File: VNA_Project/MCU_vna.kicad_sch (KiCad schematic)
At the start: 53 parts, among them J2 SWD TC2030, J401 Conn_01x04_Pin, J402 Conn_01x04_Pin, J403 Conn_01x04_Pin, J404 Conn_01x04_Pin, J5 Conn_01x04_Pin, SW401 SW_Push, SW402 SW_SPDT, U401 STM32H730VBTx, Y401 NX2016SA25MHz

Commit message: DAC
DAC
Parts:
- added R403: 2k, symbol Device:R
- added R409: 1k, symbol Device:R
- added TP401: TestPoint, symbol Connector:TestPoint
- added U402: TP17-SR, SOIC-8_TPK, symbol 2025-11-02_23-43-44:TP17-SR
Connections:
- net GND: now also R409.1, U402.4 (VS-)
- net DAC1_OUT: now reaches U401.28 (PA4)
- net DAC1_OUT: now also U402.3 (IN+)
- net USB_VBUS: no longer names the net of U401.68 (PA9)
- new net: R403.1, R409.2, U402.2 (IN-)
- new net +10V: U402.7 (VS+)
- new net VCO_TUNE: R403.2, TP401.1, U402.6 (OUT)
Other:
- note added: "Non inverting, G = 1+ R2/R1 = 3, 0-3.3V in 0-9.9V Out"
- note added: "VCO Sweep Generator"

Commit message: finishing up front end
refining Non RF front end
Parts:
- removed C18: 100nF, Capacitor_SMD:C_0402_1005Metric, symbol Device:C
- removed C415, C416: 100n, symbol Device:C
- removed D401, D402, D403, D404, D405, D406: ESD131-B1-W0201, Diode_SMD:Infineon_SG-WLL-2-3_0.58x0.28_P0.36mm, symbol Diode:ESD131-B1-W0201
- removed J2: SWD TC2030, Connector:Tag-Connect_TC2030-IDC-FP_2x03_P1.27mm_Vertical, symbol Connector:Conn_ARM_SWD_TagConnect_TC2030
- removed J401, J402: Conn_01x04_Pin, symbol Connector:Conn_01x04_Pin
- removed R404: 10k, symbol Device:R
- removed R5: 220R, Resistor_SMD:R_0402_1005Metric, symbol Device:R
- removed SW401: SW_Push, symbol Switch:SW_Push
- removed SW402: SW_SPDT, symbol Switch:SW_SPDT
- added C212: 100n, Capacitor_SMD:C_0402_1005Metric, symbol Device:C
- added C45: 100n, symbol Device:C
- added D10, D11, D12, D6, D7, D8: ESD131-B1-W0201, Diode_SMD:Infineon_SG-WLL-2-3_0.58x0.28_P0.36mm, symbol Diode:ESD131-B1-W0201
- added D13, D14, D15, D9: RED, symbol Device:LED
- added J3: 2x5 1.27mm, Connector_PinHeader_1.27mm:PinHeader_2x05_P1.27mm_Vertical_SMD, symbol Connector_Generic:Conn_02x05_Odd_Even
- added LED1: CLMVC-FKA-CL1D1L71BB7C3C3, CLMVC-FKA-CL1D1L71BB7C3C3_CRE, symbol Non_KiCad_Symbols:CLMVC-FKA-CL1D1L71BB7C3C3
- added R210, R211, R212, R213: 49R9, Resistor_SMD:R_0402_1005Metric, symbol Device:R
- added R40: 10k, Resistor_SMD:R_1206_3216Metric_Pad1.30x1.75mm_HandSolder, symbol Device:R
- added R41, R42, R43, R44, R45, R46: 1000, symbol Device:R
- added SW3: SW_SPDT, Button_Switch_THT:SW_Slide_SPDT_Straight_CK_OS102011MS2Q, symbol Switch:SW_SPDT
- R6: value 220R -> 1000; footprint Resistor_SMD:R_0402_1005Metric -> (none)
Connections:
- net UART_RX is gone; now on net GND: R6.2
- net +3.3V: now also C45.1, D10.2 (A2), D11.2 (A2), D12.2 (A2), D6.2 (A2), J3.1 (Pin_1), LED1.1, SW3.3 (C)
- net BOOT0: now also R40.1
- net GND: now also C212.2, C45.2, D10.1 (A1), D11.1 (A1), D12.1 (A1), D6.1 (A1), D7.1 (A1), D8.1 (A1), J3.3 (Pin_3), J3.5 (Pin_5), J3.9 (Pin_9), R41.2, R42.2, R43.2, SW3.1 (A)
- net JTDO: now also R212.1
- net NRST: now also C212.1, R213.1
- net SWCLK: now also R211.1; no longer D3.2 (A2)
- net SWDIO: now also R210.1; no longer D2.2 (A2)
- net debug_led2: now reaches U401.34 (PB0)
- net debug_led2: now also D13.2 (A)
- net debug_led3: now reaches U401.35 (PB1)
- net debug_led3: now also D14.2 (A)
- net debug_led4: now reaches U401.36 (PB2)
- net debug_led4: now also D15.2 (A)
- net debug_led6: now reaches U401.91 (PB5)
- net debug_led6: now also R45.1
- net debug_led7: now reaches U401.95 (PB8)
- net debug_led7: now also R46.1
- net at R6.1: now also D9.1 (K)
- net JTDI renamed debug_led1
- net debug_led1: now also D9.2 (A)
- net JTRST renamed debug_led5
- net debug_led5: now also R44.1
- new net: D14.1 (K), R42.1
- new net: D13.1 (K), R41.1
- new net: LED1.2, R46.2
- new net: D15.1 (K), R43.1
- new net: LED1.4, R44.2
- new net: LED1.3, R45.2
- new net: R40.2, SW3.2 (B)
- new net CONN_NRST: D8.2 (A2), J3.10 (Pin_10), R213.2
- new net CONN_SWCLK: D3.2 (A2), J3.4 (Pin_4), R211.2
- new net CONN_SWDIO: D2.2 (A2), J3.2 (Pin_2), R210.2
- new net CONN_SWO: D7.2 (A2), J3.6 (Pin_6), R212.2
- no-connect marks 1 -> 33
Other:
- note added: "- credit phils lab"
- note added: "1k"
- note added: "25MHZ"
- note added: "DEBUG 1 - Clock DEBUG 2 - ADC DEBUG 3 - DAC DEBUG 4 - ETH DEBUG 5,6,7 - Temperature Stability Gradient"
- note added: "RGB Gradient"
- note removed: "NRST"
- note removed: "SWD 2"
- note removed: "UART"
- moved on the sheet: D407, D408, D409, D410, D411, D412, J403, J404, J5, R403, R405, R406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

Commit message: AA filtering
redoing AA filtering
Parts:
- removed D10, D11, D12, D407, D408, D409, D410, D411, D412: ESD131-B1-W0201, Diode_SMD:Infineon_SG-WLL-2-3_0.58x0.28_P0.36mm, symbol Diode:ESD131-B1-W0201
- removed J403, J404, J5: Conn_01x04_Pin, Connector_PinSocket_2.00mm:PinSocket_1x04_P2.00mm_Vertical, symbol Connector:Conn_01x04_Pin
- removed R405, R406, R407, R408, R8, R9: 1.5K, Resistor_SMD:R_0402_1005Metric, symbol Device:R
- removed TP401: TestPoint, symbol Connector:TestPoint
- added C48: 100n, symbol Device:C
- added D10: RED, symbol Device:LED
- added J7: Screw_Terminal_01x02, symbol Connector:Screw_Terminal_01x02
- added R47, R48, R49, R50, R51, R52, R53, R54, R55: 1.5K, Resistor_SMD:R_0402_1005Metric, symbol Device:R
- added R56: 1000, symbol Device:R
- added U12, U13, U14: TMP75AID, D8, symbol Non_KiCad_Symbols:TMP75AID
- C413, C414: value 5.6p -> 10p
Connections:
- net +10V: now also C48.1
- net +3.3V: now also R47.1, R48.1, R49.1, R50.1, R51.1, R52.1, R53.1, R54.1, R55.1, U12.8 (V+), U13.8 (V+), U14.8 (V+)
- net GND: now also C48.2, J7.2 (Pin_2), R56.2, U12.4 (GND), U12.5 (A2), U12.6 (A1), U12.7 (A0), U13.4 (GND), U13.5 (A2), U13.6 (A1), U13.7 (A0), U14.4 (GND), U14.5 (A2), U14.6 (A1), U14.7 (A0)
- net I2C1_SCL: now also R48.2, U12.2 (SCL)
- net I2C1_SDA: now also R47.2, U12.1 (SDA)
- net I2C4_SCL: now also R51.2, U13.2 (SCL)
- net I2C4_SDA: now also R50.2, U13.1 (SDA)
- net I2C5_SCL: now also R54.2, U14.2 (SCL)
- net I2C5_SDA: now also R53.2, U14.1 (SDA)
- net VCO_TUNE: now also J7.1 (Pin_1)
- net alerttemp1: now reaches U401.61 (PD14)
- net alerttemp1: now also R49.2, U12.3 (ALERT)
- net alerttemp2: now reaches U401.62 (PD15)
- net alerttemp2: now also R52.2, U13.3 (ALERT)
- net alerttemp3: now reaches U401.9 (PC15)
- net alerttemp3: now also R55.2, U14.3 (ALERT)
- net debug_led8: now reaches U401.96 (PB9)
- net debug_led8: now also D10.2 (A)
- new net: D10.1 (K), R56.1
- no-connect marks 33 -> 29
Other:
- note added: "12 bit DAC out gives 3.3V / 2^n resolution step size IN -> step size out = ( 3.3V / 2^n ) * Gain = 2 mV step size for a 0- 9.9V sweep"
- note added: "Cs = 3pF 8 CL = C/2 +3 2*5pF = C C = 10pF"
- note added: "DEBUG 1 - Clock DEBUG 2 - ADC DEBUG 3 - DAC DEBUG 4 - ETH DEBUG 5,6,7 - Temperature Stability Gradient DEBUG 8 - Calibration Status"
- note added: "Temp gradient 1"
- note added: "Temp gradient 2"
- note added: "Temp gradient 3"
- note removed: "2 - I2C4"
- note removed: "3 - I2C5"
- note removed: "DEBUG 1 - Clock DEBUG 2 - ADC DEBUG 3 - DAC DEBUG 4 - ETH DEBUG 5,6,7 - Temperature Stability Gradient"
- note removed: "I2C1"
- moved on the sheet: C45, D13, D14, D15, D9, LED1, R403, R409, R41, R42, R43, R44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

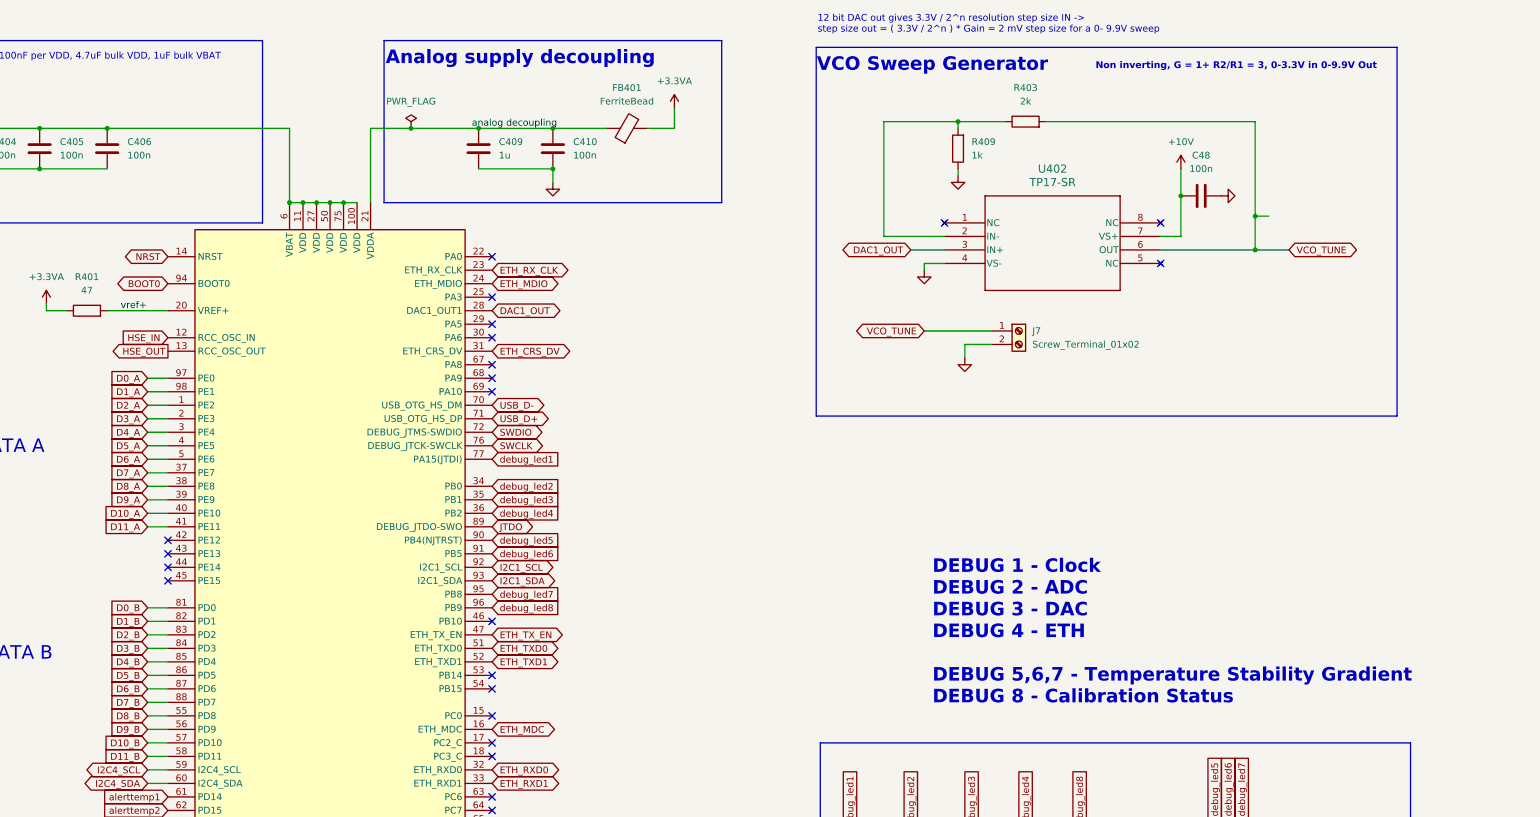
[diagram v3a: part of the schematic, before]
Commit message: VNA V1
FRONT END  FIRST PROTOTYPE SCHEMATIC DONE
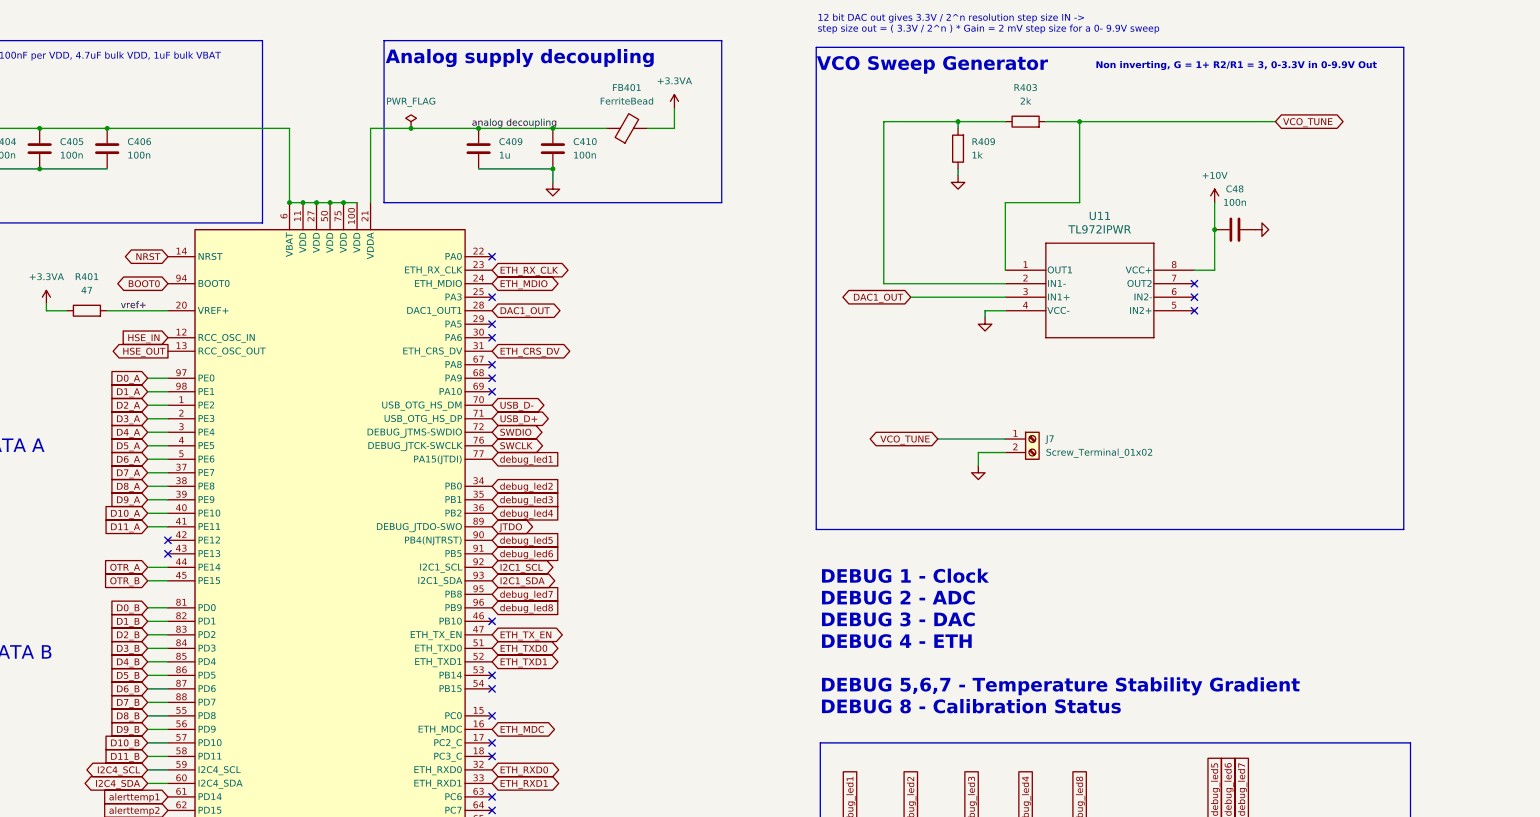
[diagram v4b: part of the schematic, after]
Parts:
- removed U402: TP17-SR, SOIC-8_TPK, symbol 2025-11-02_23-43-44:TP17-SR
- added U11: TL972IPWR, PW8, symbol Non_KiCad_Symbols:TL972IPWR
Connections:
- net +10V: now also U11.8 (VCC+)
- net DAC1_OUT: now also U11.3 (IN1+)
- net GND: now also U11.4 (VCC-)
- net VCO_TUNE: now also U11.1 (OUT1)
- net OTR_A: now reaches U401.44 (PE14)
- net OTR_B: now reaches U401.45 (PE15)
- net at R403.1, R409.2: now also U11.2 (IN1-)
- no-connect marks 29 -> 27
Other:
- moved on the sheet: C48, J7

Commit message: footprints + initial layout shape
footprints + initial layout shape
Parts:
- added H301, H302, H303, H304: MountingHole, MountingHole:MountingHole_2.2mm_M2, symbol Mechanical:MountingHole
- C301: renamed from C413; footprint (none) -> Capacitor_SMD:C_0603_1608Metric_Pad1.08x0.95mm_HandSolder
- C302: renamed from C408; footprint (none) -> Capacitor_SMD:C_0603_1608Metric_Pad1.08x0.95mm_HandSolder
- C303: renamed from C407; footprint (none) -> Capacitor_SMD:C_0603_1608Metric_Pad1.08x0.95mm_HandSolder
- C304: renamed from C414; footprint (none) -> Capacitor_SMD:C_0603_1608Metric_Pad1.08x0.95mm_HandSolder
- C305: renamed from C401; footprint (none) -> Capacitor_SMD:C_0603_1608Metric_Pad1.08x0.95mm_HandSolder
- C306: renamed from C212; footprint Capacitor_SMD:C_0402_1005Metric -> Capacitor_SMD:C_0603_1608Metric_Pad1.08x0.95mm_HandSolder
- C307: renamed from C402; footprint (none) -> Capacitor_SMD:C_0603_1608Metric_Pad1.08x0.95mm_HandSolder
- C308: renamed from C403; footprint (none) -> Capacitor_SMD:C_0603_1608Metric_Pad1.08x0.95mm_HandSolder
- C309: renamed from C404; footprint (none) -> Capacitor_SMD:C_0603_1608Metric_Pad1.08x0.95mm_HandSolder
- C310: renamed from C412; footprint (none) -> Capacitor_SMD:C_0603_1608Metric_Pad1.08x0.95mm_HandSolder
- C311: renamed from C405; footprint (none) -> Capacitor_SMD:C_0603_1608Metric_Pad1.08x0.95mm_HandSolder
- C312: renamed from C411; footprint (none) -> Capacitor_SMD:C_0603_1608Metric_Pad1.08x0.95mm_HandSolder
- C313: renamed from C406; footprint (none) -> Capacitor_SMD:C_0603_1608Metric_Pad1.08x0.95mm_HandSolder
- C314: renamed from C409; footprint (none) -> Capacitor_SMD:C_0603_1608Metric_Pad1.08x0.95mm_HandSolder
- C315: renamed from C410; footprint (none) -> Capacitor_SMD:C_0603_1608Metric_Pad1.08x0.95mm_HandSolder
- C316: renamed from C45; footprint (none) -> Capacitor_SMD:C_0603_1608Metric_Pad1.08x0.95mm_HandSolder
- C317: renamed from C48; footprint (none) -> Capacitor_SMD:C_0603_1608Metric_Pad1.08x0.95mm_HandSolder
- D306: renamed from D9; footprint (none) -> LED_SMD:LED_0603_1608Metric_Pad1.05x0.95mm_HandSolder
- D307: renamed from D13; footprint (none) -> LED_SMD:LED_0603_1608Metric_Pad1.05x0.95mm_HandSolder
- D308: renamed from D14; footprint (none) -> LED_SMD:LED_0603_1608Metric_Pad1.05x0.95mm_HandSolder
- D309: renamed from D15; footprint (none) -> LED_SMD:LED_0603_1608Metric_Pad1.05x0.95mm_HandSolder
- D310: renamed from D10; footprint (none) -> LED_SMD:LED_0603_1608Metric_Pad1.05x0.95mm_HandSolder
- FB301: renamed from FB401; footprint (none) -> Inductor_SMD:L_0603_1608Metric_Pad1.05x0.95mm_HandSolder
- J301: renamed from J3; footprint Connector_PinHeader_1.27mm:PinHeader_2x05_P1.27mm_Vertical_SMD -> Connector_PinHeader_2.54mm:PinHeader_2x05_P2.54mm_Vertical
- J302: renamed from J7; footprint (none) -> TerminalBlock:TerminalBlock_MaiXu_MX126-5.0-02P_1x02_P5.00mm
- LED301: renamed from LED1; footprint CLMVC-FKA-CL1D1L71BB7C3C3_CRE -> NonKiCad_footprints:CLMVC-FKA-CL1D1L71BB7C3C3_CRE
- R301: renamed from R47; footprint Resistor_SMD:R_0402_1005Metric -> Resistor_SMD:R_0603_1608Metric_Pad0.98x0.95mm_HandSolder
- R302: renamed from R40; footprint Resistor_SMD:R_1206_3216Metric_Pad1.30x1.75mm_HandSolder -> Resistor_SMD:R_0603_1608Metric_Pad0.98x0.95mm_HandSolder
- R303: renamed from R48; footprint Resistor_SMD:R_0402_1005Metric -> Resistor_SMD:R_0603_1608Metric_Pad0.98x0.95mm_HandSolder
- R304: renamed from R49; footprint Resistor_SMD:R_0402_1005Metric -> Resistor_SMD:R_0603_1608Metric_Pad0.98x0.95mm_HandSolder
- R305: renamed from R402; footprint (none) -> Resistor_SMD:R_0603_1608Metric_Pad0.98x0.95mm_HandSolder
- R306: renamed from R210; footprint Resistor_SMD:R_0402_1005Metric -> Resistor_SMD:R_0603_1608Metric_Pad0.98x0.95mm_HandSolder
- R307: renamed from R211; footprint Resistor_SMD:R_0402_1005Metric -> Resistor_SMD:R_0603_1608Metric_Pad0.98x0.95mm_HandSolder
- R308: renamed from R212; footprint Resistor_SMD:R_0402_1005Metric -> Resistor_SMD:R_0603_1608Metric_Pad0.98x0.95mm_HandSolder
- R309: renamed from R213; footprint Resistor_SMD:R_0402_1005Metric -> Resistor_SMD:R_0603_1608Metric_Pad0.98x0.95mm_HandSolder
- R310: renamed from R50; footprint Resistor_SMD:R_0402_1005Metric -> Resistor_SMD:R_0603_1608Metric_Pad0.98x0.95mm_HandSolder
- R311: renamed from R51; footprint Resistor_SMD:R_0402_1005Metric -> Resistor_SMD:R_0603_1608Metric_Pad0.98x0.95mm_HandSolder
- R312: renamed from R52; footprint Resistor_SMD:R_0402_1005Metric -> Resistor_SMD:R_0603_1608Metric_Pad0.98x0.95mm_HandSolder
- R313: renamed from R401; footprint (none) -> Resistor_SMD:R_0603_1608Metric_Pad0.98x0.95mm_HandSolder
- R314: renamed from R53; footprint Resistor_SMD:R_0402_1005Metric -> Resistor_SMD:R_0603_1608Metric_Pad0.98x0.95mm_HandSolder
- R315: renamed from R54; footprint Resistor_SMD:R_0402_1005Metric -> Resistor_SMD:R_0603_1608Metric_Pad0.98x0.95mm_HandSolder
- R316: renamed from R55; footprint Resistor_SMD:R_0402_1005Metric -> Resistor_SMD:R_0603_1608Metric_Pad0.98x0.95mm_HandSolder
- R317: renamed from R6; footprint (none) -> Resistor_SMD:R_0603_1608Metric_Pad0.98x0.95mm_HandSolder
- R318: renamed from R41; footprint (none) -> Resistor_SMD:R_0603_1608Metric_Pad0.98x0.95mm_HandSolder
- R319: renamed from R409; footprint (none) -> Resistor_SMD:R_0603_1608Metric_Pad0.98x0.95mm_HandSolder
- R320: renamed from R42; footprint (none) -> Resistor_SMD:R_0603_1608Metric_Pad0.98x0.95mm_HandSolder
- R321: renamed from R403; footprint (none) -> Resistor_SMD:R_0603_1608Metric_Pad0.98x0.95mm_HandSolder
- R322: renamed from R43; footprint (none) -> Resistor_SMD:R_0603_1608Metric_Pad0.98x0.95mm_HandSolder
- R323: renamed from R56; footprint (none) -> Resistor_SMD:R_0603_1608Metric_Pad0.98x0.95mm_HandSolder
- R324: renamed from R44; footprint (none) -> Resistor_SMD:R_0603_1608Metric_Pad0.98x0.95mm_HandSolder
- R325: renamed from R45; footprint (none) -> Resistor_SMD:R_0603_1608Metric_Pad0.98x0.95mm_HandSolder
- R326: renamed from R46; footprint (none) -> Resistor_SMD:R_0603_1608Metric_Pad0.98x0.95mm_HandSolder
- U301: renamed from U12; footprint D8 -> NonKiCad_footprints:TMP75AID
- U302: renamed from U13; footprint D8 -> NonKiCad_footprints:TMP75AID
- U304: renamed from U14; footprint D8 -> NonKiCad_footprints:TMP75AID
- U305: renamed from U11; footprint PW8 -> NonKiCad_footprints:TL972IPWR
- Y301: renamed from Y401; value NX2016SA25MHz -> STDCZS1-25M; footprint (none) -> Crystal:Crystal_SMD_2016-4Pin_2.0x1.6mm
- renumbered D6 to D301, D2 to D302, D3 to D303, D7 to D304, D8 to D305, SW3 to SW301, U401 to U303

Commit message: Layout
Layout
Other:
- moved on the sheet: H301

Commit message: DRC silkscreen
fixed DRC and silkscreen
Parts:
- D301, D302, D303, D304, D305: footprint Diode_SMD:Infineon_SG-WLL-2-3_0.58x0.28_P0.36mm -> Diode_SMD:Nexperia_DSN0603-2_0.6x0.3mm_P0.4mm
